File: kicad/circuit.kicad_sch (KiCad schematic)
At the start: 20 parts, among them SW1 {dblquote}Snap wire{dblquote}, U1 74HC595

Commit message: Add system diagram and reexport all diagrams.
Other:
- title: Circuit diagrams for pico-rio. -> Circuit diagram for pico-rio
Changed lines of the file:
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@@
 	(paper "A4")
 	(title_block
-		(title "Circuit diagrams for pico-rio.")
+		(title "Circuit diagram for pico-rio")
 		(date "2026-06-12")
 		(rev "0")

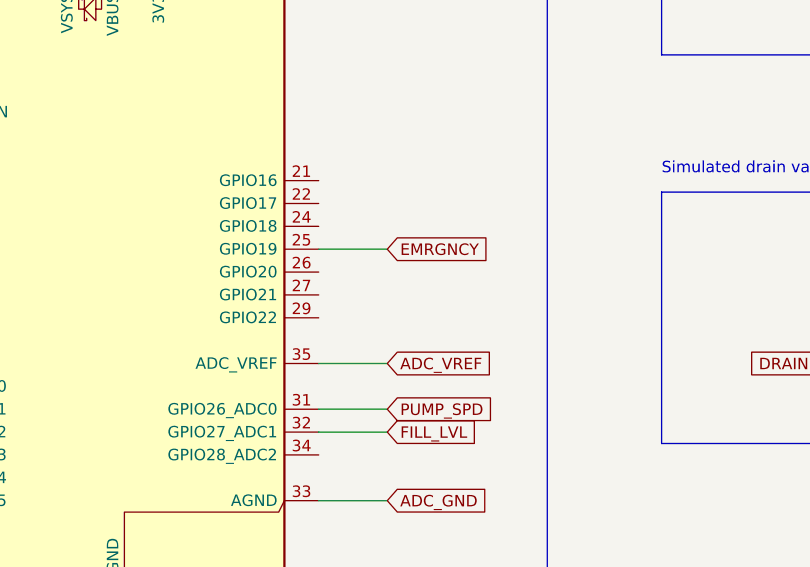
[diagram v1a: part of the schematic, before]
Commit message: Fix bugs in diagrams.
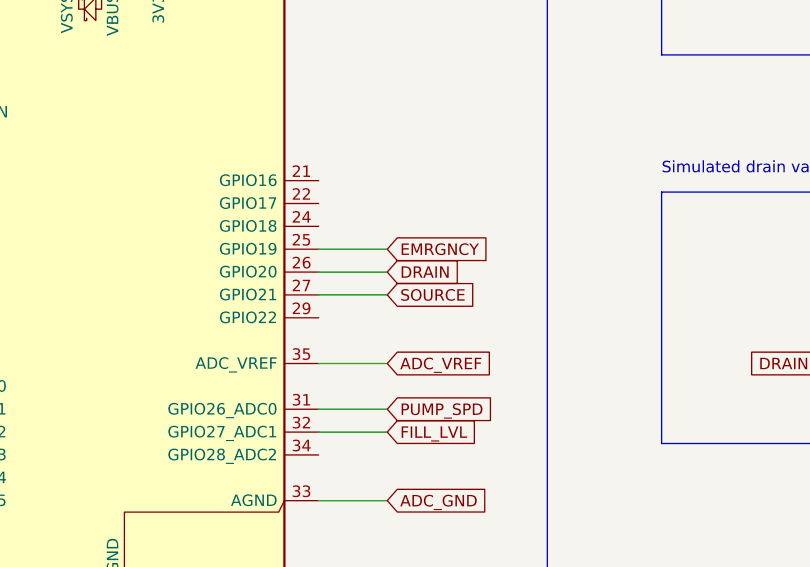
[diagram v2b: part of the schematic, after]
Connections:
- net DRAIN: now also A1.26 (GPIO20)
- net SOURCE: now also A1.27 (GPIO21)
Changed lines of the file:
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@@
+	(wire
+		(pts
+			(xy 92.71 73.66) (xy 100.33 73.66)
+		)
+		(stroke
+			(width 0)
+			(type default)
+		)
+	)
 	(wire
 		(pts
@@
 	(wire
 		(pts
+			(xy 100.33 71.12) (xy 92.71 71.12)
+		)
+		(stroke
+			(width 0)
+			(type default)
+		)
+	)
+	(wire
+		(pts
 			(xy 66.04 170.18) (xy 72.39 170.18)
 		)
@@
 		)
 	)
+	(global_label "SOURCE"
+		(shape input)
+		(at 100.33 73.66 0)
+		(fields_autoplaced yes)
+		(effects
+			(font
+				(size 1.27 1.27)
+			)
+			(justify left)
+		)
+		(property "Intersheetrefs" "${INTERSHEET_REFS}"
+			(at 110.8747 73.66 0)
+			(effects
+				(font
+					(size 1.27 1.27)
+				)
+				(justify left)
+				(hide yes)
+			)
+		)
+	)
 	(global_label "3.3_V"
 		(shape input)
@@
 				(hide yes)
 			)
+		)
+	)
+	(global_label "DRAIN"
+		(shape input)
+		(at 100.33 71.12 0)
+		(fields_autoplaced yes)
+		(effects
+			(font
+				(size 1.27 1.27)
+			)
+			(justify left)
+		)
+		(property "Intersheetrefs" "${INTERSHEET_REFS}"
+			(at 108.8791 71.12 0)
+			(effects
+				(font
+					(size 1.27 1.27)
+				)
+				(justify left)
+				(hide yes)
+			)

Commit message: Update README and diagrams.
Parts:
- renumbered A1 to U1, U1 to U2
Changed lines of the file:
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@@
 		(dnp no)
 		(fields_autoplaced yes)
-		(property "Reference" "A1"
+		(property "Reference" "U1"
 			(at 71.9933 107.95 0)
 			(effects
@@
 			(project "circuit"
 				(path "/ab48db55-0259-4fd2-a900-3952423ed41a"
-					(reference "A1")
+					(reference "U1")
 					(unit 1)
 				)
@@
 		(dnp no)
 		(fields_autoplaced yes)
-		(property "Reference" "U1"
+		(property "Reference" "U2"
 			(at 58.0233 144.78 0)
 			(effects
@@
 			(project "circuit"
 				(path "/ab48db55-0259-4fd2-a900-3952423ed41a"
-					(reference "U1")
-					(unit 1)
-				)
+					(reference "U2")
+					(unit 1)
+				)

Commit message: Update schematic and diagram.
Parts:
- removed BAR1: Bar graph, Display:HDSP-4830, symbol LED:HDSP-4830_2
- removed D1: Source valve, symbol Device:LED
- removed D2: Drain valve, symbol Device:LED
- removed R10, R11, R12, R3, R4, R5, R6, R7, R8, R9: 330, symbol Device:R
- removed U2: 74HC595, symbol 74xx:74HC595
- added OLED1: ssd1306, symbol pico-rio:ssd1306
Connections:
- net 3.3_V: now also OLED1.1 (VCC)
- net EMRGNCY: now also U1.27 (GPIO21); no longer U1.25 (GPIO19)
- net GND: now also OLED1.2 (GND)
- net nRES: now reaches U1.1 (GPIO0)
- net nRES: now also OLED1.8 (nRES)
- net DRAIN_IN: now reaches U1.16 (GPIO12)
- net DRAIN_IN: now also U1.25 (GPIO19)
- net D/C: now reaches U1.2 (GPIO1)
- net D/C: now also OLED1.7 (D/C)
- net SPI0_nCS: now reaches U1.7 (GPIO5)
- net SPI0_nCS: now also OLED1.6 (nCS)
- net 5_V: no longer names the net of U1.39 (VSYS)
- net BAR_CLK renamed SPI0_CLK
- net SPI0_CLK: now also OLED1.5 (CLK)
- net BAR_DATA: no longer names the net of U1.6 (GPIO4)
- net BAR_LTCH renamed SPI0_TX
- net SPI0_TX: now also OLED1.4 (DIN)
- net DRAIN renamed SRC_IN
- net SOURCE: no longer names the net of U1.14 (GPIO10)
- net SOURCE: no longer U1.27 (GPIO21)
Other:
- note added: "Drain valve (normally open, simulated, feedback = actuation)"
- note added: "OLED display"
- note added: "Source valve (normally closed, simulated, feedback = actuation)"
- note removed: "LED bar graph"
- note removed: "R5-R12 330"
- note removed: "Simulated drain valve (normally open, open when LED is on)"
- note removed: "Simulated source valve (normally closed, open when LED is on)"
